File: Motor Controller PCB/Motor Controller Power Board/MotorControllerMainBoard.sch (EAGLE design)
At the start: 59 parts, among them U1 CDBA340L-G

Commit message: Started board work
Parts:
- removed C7, C8: EEUFR1H221B, MotorControllerEagleLibrary:EEUFR1H221B
- removed LED3: (no value), SparkFun (2015_10_14 22_27_04 UTC):LED1206
- removed R12, R9: FKN1WSJR-52-4R7, MotorControllerEagleLibrary:FKN1WSJR-52-4R7
- removed SV1, SV3, SV4: (no value), con-lstb:MA03-1
- removed U$21: (no value), MotorControllerEagleLibrary:AL5809-20S1-7
- added U$24: DA-T263-101E, MotorControllerEagleLibrary:DA-T263-101E
- added U$25: LTN20069, MotorControllerEagleLibrary:LTN20069
- SV2: device con-lstb:MA03-1 -> con-lstb:MA04-1
- U$1, U$2: value NTMFS5C426NT1G -> IPB015N08N5ATMA1; device MotorControllerEagleLibrary:NTMFS5C426NT1G -> MotorControllerEagleLibrary:IPB015N08N5ATMA1
- U$3, U$4: value NTMFS5C426NT1G -> DA-T263-101E; device MotorControllerEagleLibrary:NTMFS5C426NT1G -> MotorControllerEagleLibrary:DA-T263-101E
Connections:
- removed net N$11: R9.22, U$3.GATE
- removed net N$12: R12.22, U$4.GATE
- removed net N$13: R9.11, SV2.2
- removed net N$3: R10.11, SV1.2
- removed net N$4: LED3.C, U$21.A
- removed net N$5: R12.11, SV3.2
- removed net N$8: R11.11, SV4.2
- net 12V_POWER_REGULATED: no longer C7.POSITIVE, C8.POSITIVE
- net 3.3V_ISOLATED: no longer LED3.A
- net FET_DRIVER_SIGNAL: now also R10.11, R11.11; no longer SV1.3, SV2.3, SV3.3, SV4.3
- net GND: now also U$24.GND; no longer C7.NEGATIVE, C8.NEGATIVE, SV1.1, SV2.1, SV3.1, SV6.1, SV6.2, SV6.3, SV6.4, SV7.1, SV7.2, SV7.3, SV7.4, U$3.SOURCE\, U$4.SOURCE\
- net GND_ISOLATED: no longer U$21.C
- net INPUT_POWER(+): now also U$23.GND
- net MOTOR_OUTPUT_(--): now also U$3.GND, U$4.GND; no longer U$3.DRAIN, U$4.DRAIN
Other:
- note added: "HeatSink"

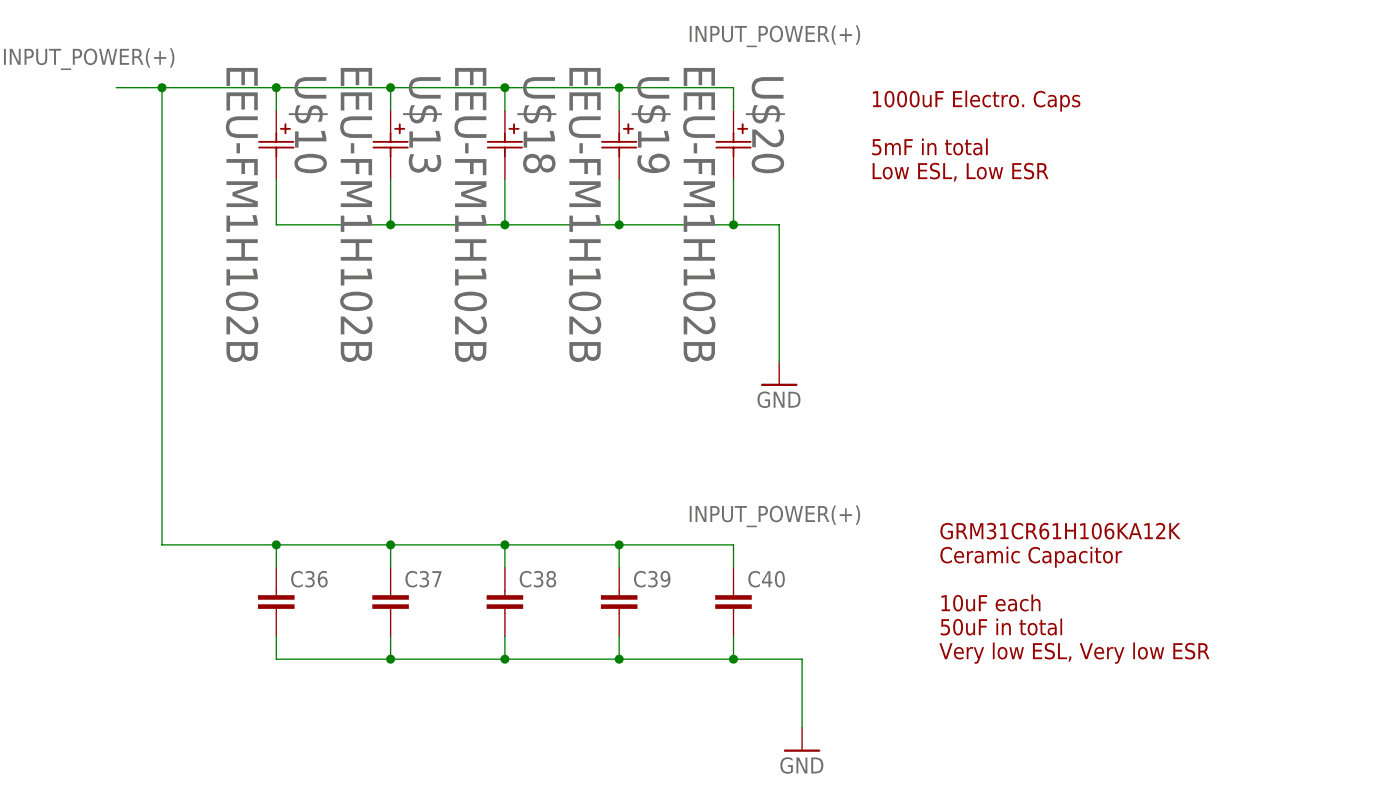
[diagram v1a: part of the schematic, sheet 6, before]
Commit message: shrunk board size to 10x6cm
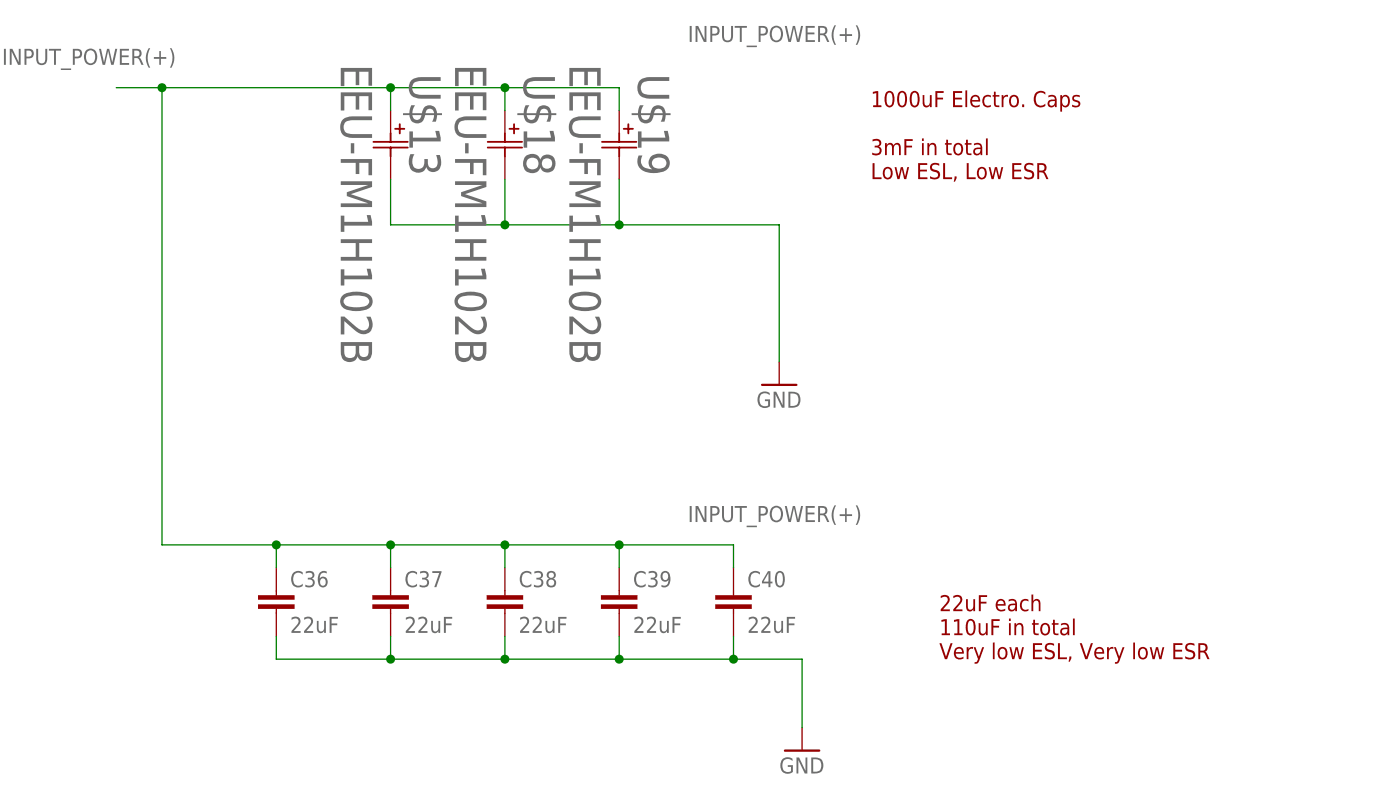
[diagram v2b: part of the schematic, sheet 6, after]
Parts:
- removed U$10, U$20: EEU-FM1H102B, MotorControllerEagleLibrary:EEU-FM1H102B
- C36, C37, C38, C39, C40: value (none) -> 22uF; device resistor:C-EUC1206 -> rcl:C-EUC1210
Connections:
- net GND: no longer U$10.NEGATIVE, U$20.NEGATIVE
- net INPUT_POWER(+): no longer U$10.POSITIVE, U$20.POSITIVE
- net MOTOR_OUTPUT_(+): now also U$9.4; no longer U$9.5
- net POWER_INPUT(+): now also U$9.5; no longer U$9.4
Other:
- note added: "1000uF Electro. Caps 3mF in total Low ESL, Low ESR"
- note added: "22uF each 110uF in total Very low ESL, Very low ESR"
- note removed: "1000uF Electro. Caps 5mF in total Low ESL, Low ESR"
- note removed: "GRM31CR61H106KA12K Ceramic Capacitor 10uF each 50uF in total Very low ESL, Very low ESR"
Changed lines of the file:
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@@
 <part name="GND23" library="E-P-008-R1.2" deviceset="GND" device=""/>
 <part name="GND24" library="SparkFun-Aesthetics" deviceset="GND" device=""/>
-<part name="C36" library="resistor" library_urn="urn:adsk.eagle:library:348" deviceset="C-EU" device="C1206" package3d_urn="urn:adsk.eagle:package:26140/1"/>
-<part name="C37" library="resistor" library_urn="urn:adsk.eagle:library:348" deviceset="C-EU" device="C1206" package3d_urn="urn:adsk.eagle:package:26140/1"/>
-<part name="C38" library="resistor" library_urn="urn:adsk.eagle:library:348" deviceset="C-EU" device="C1206" package3d_urn="urn:adsk.eagle:package:26140/1"/>
-<part name="C39" library="resistor" library_urn="urn:adsk.eagle:library:348" deviceset="C-EU" device="C1206" package3d_urn="urn:adsk.eagle:package:26140/1"/>
-<part name="C40" library="resistor" library_urn="urn:adsk.eagle:library:348" deviceset="C-EU" device="C1206" package3d_urn="urn:adsk.eagle:package:26140/1"/>
+<part name="C36" library="rcl" library_urn="urn:adsk.eagle:library:334" deviceset="C-EU" device="C1210" package3d_urn="urn:adsk.eagle:package:23619/2" value="22uF"/>
+<part name="C37" library="rcl" library_urn="urn:adsk.eagle:library:334" deviceset="C-EU" device="C1210" package3d_urn="urn:adsk.eagle:package:23619/2" value="22uF"/>
+<part name="C38" library="rcl" library_urn="urn:adsk.eagle:library:334" deviceset="C-EU" device="C1210" package3d_urn="urn:adsk.eagle:package:23619/2" value="22uF"/>
+<part name="C39" library="rcl" library_urn="urn:adsk.eagle:library:334" deviceset="C-EU" device="C1210" package3d_urn="urn:adsk.eagle:package:23619/2" value="22uF"/>
+<part name="C40" library="rcl" library_urn="urn:adsk.eagle:library:334" deviceset="C-EU" device="C1210" package3d_urn="urn:adsk.eagle:package:23619/2" value="22uF"/>
 <part name="GND25" library="SparkFun-Aesthetics" deviceset="GND" device=""/>
 <part name="U$12" library="Connector 732-3204" deviceset="732-3204-ND_CONNECTOR" device=""/>
@@
 <part name="PWR_CONFIRM" library="led" library_urn="urn:adsk.eagle:library:259" deviceset="LED" device="CHIPLED_1206" package3d_urn="urn:adsk.eagle:package:15823/2" value="RED"/>
 <part name="GND22" library="E-P-008-R1.2" deviceset="GND" device=""/>
-<part name="U$10" library="MotorControllerEagleLibrary" deviceset="EEU-FM1H102B" device=""/>
 <part name="U$13" library="MotorControllerEagleLibrary" deviceset="EEU-FM1H102B" device=""/>
 <part name="U$18" library="MotorControllerEagleLibrary" deviceset="EEU-FM1H102B" device=""/>
 <part name="U$19" library="MotorControllerEagleLibrary" deviceset="EEU-FM1H102B" device=""/>
-<part name="U$20" library="MotorControllerEagleLibrary" deviceset="EEU-FM1H102B" device=""/>
 <part name="U$8" library="MotorControllerEagleLibrary" deviceset="AL5809-20S1-7" device=""/>
 <part name="LED2" library="SparkFun (2015_10_14 22_27_04 UTC)" deviceset="LED" device="1206"/>
@@
 <net name="POWER_INPUT(+)" class="0">
 <segment>
-<pinref part="U$9" gate="G$1" pin="4"/>
-<wire x1="144.78" y1="83.82" x2="144.78" y2="71.12" width="0.1524" layer="91"/>
-<label x="129.54" y="68.58" size="1.778" layer="95"/>
-</segment>
-</net>
-<net name="MOTOR_OUTPUT_(+)" class="0">
-<segment>
 <pinref part="U$9" gate="G$1" pin="5"/>
 <wire x1="160.02" y1="83.82" x2="160.02" y2="71.12" width="0.1524" layer="91"/>
@@
 <wire x1="175.26" y1="109.22" x2="175.26" y2="106.68" width="0.1524" layer="91"/>
 <label x="175.26" y="104.14" size="1.778" layer="95"/>
+</segment>
+</net>
+<net name="MOTOR_OUTPUT_(+)" class="0">
+<segment>
+<pinref part="U$9" gate="G$1" pin="4"/>
+<wire x1="144.78" y1="83.82" x2="144.78" y2="71.12" width="0.1524" layer="91"/>
+<label x="129.54" y="68.58" size="1.778" layer="95"/>
 </segment>
 </net>
@@
 <plain>
 <text x="195.58" y="27.94" size="3.81" layer="94">Input Filters</text>
-<text x="114.3" y="96.52" size="1.778" layer="94">GRM31CR61H106KA12K
-Ceramic Capacitor
-10uF each
-50uF in total
+<text x="114.3" y="96.52" size="1.778" layer="94">22uF each
+110uF in total
 Very low ESL, Very low ESR</text>
 <text x="106.68" y="149.86" size="1.778" layer="94">1000uF Electro. Caps
-5mF in total
+3mF in total
 Low ESL, Low ESR</text>
 </plain>
@@
 <instance part="C40" gate="G$1" x="91.44" y="104.14"/>
 <instance part="GND25" gate="1" x="99.06" y="86.36"/>
-<instance part="U$10" gate="G$1" x="40.64" y="157.48" rot="R270"/>
 <instance part="U$13" gate="G$1" x="53.34" y="157.48" rot="R270"/>
 <instance part="U$18" gate="G$1" x="66.04" y="157.48" rot="R270"/>
 <instance part="U$19" gate="G$1" x="78.74" y="157.48" rot="R270"/>
-<instance part="U$20" gate="G$1" x="91.44" y="157.48" rot="R270"/>
 </instances>
 <busses>
@@
 <net name="INPUT_POWER(+)" class="0">
 <segment>
-<wire x1="40.64" y1="157.48" x2="40.64" y2="160.02" width="0.1524" layer="91"/>
-<wire x1="40.64" y1="160.02" x2="53.34" y2="160.02" width="0.1524" layer="91"/>
 <wire x1="53.34" y1="160.02" x2="66.04" y2="160.02" width="0.1524" layer="91"/>
 <wire x1="66.04" y1="160.02" x2="78.74" y2="160.02" width="0.1524" layer="91"/>
-<wire x1="78.74" y1="160.02" x2="91.44" y2="160.02" width="0.1524" layer="91"/>
 <wire x1="53.34" y1="160.02" x2="53.34" y2="157.48" width="0.1524" layer="91"/>
 <junction x="53.34" y="160.02"/>
@@
 <junction x="66.04" y="160.02"/>
 <wire x1="78.74" y1="160.02" x2="78.74" y2="157.48" width="0.1524" layer="91"/>
-<junction x="78.74" y="160.02"/>
-<wire x1="91.44" y1="160.02" x2="91.44" y2="157.48" width="0.1524" layer="91"/>
-<wire x1="40.64" y1="160.02" x2="27.94" y2="160.02" width="0.1524" layer="91"/>
-<junction x="40.64" y="160.02"/>
+<wire x1="53.34" y1="160.02" x2="27.94" y2="160.02" width="0.1524" layer="91"/>
 <label x="10.16" y="162.56" size="1.778" layer="95"/>
 <wire x1="27.94" y1="160.02" x2="22.86" y2="160.02" width="0.1524" layer="91"/>
@@
 <label x="86.36" y="111.76" size="1.778" layer="95"/>
 <label x="86.36" y="165.1" size="1.778" layer="95"/>
-<pinref part="U$10" gate="G$1" pin="POSITIVE"/>
 <pinref part="U$13" gate="G$1" pin="POSITIVE"/>
 <pinref part="U$18" gate="G$1" pin="POSITIVE"/>
 <pinref part="U$19" gate="G$1" pin="POSITIVE"/>
-<pinref part="U$20" gate="G$1" pin="POSITIVE"/>
 </segment>
 </net>
 <net name="GND" class="0">
 <segment>
-<wire x1="40.64" y1="149.86" x2="40.64" y2="144.78" width="0.1524" layer="91"/>
-<wire x1="40.64" y1="144.78" x2="53.34" y2="144.78" width="0.1524" layer="91"/>
 <wire x1="53.34" y1="144.78" x2="66.04" y2="144.78" width="0.1524" layer="91"/>
 <wire x1="66.04" y1="144.78" x2="78.74" y2="144.78" width="0.1524" layer="91"/>
-<wire x1="78.74" y1="144.78" x2="91.44" y2="144.78" width="0.1524" layer="91"/>
-<wire x1="91.44" y1="144.78" x2="96.52" y2="144.78" width="0.1524" layer="91"/>
+<wire x1="78.74" y1="144.78" x2="96.52" y2="144.78" width="0.1524" layer="91"/>
 <wire x1="53.34" y1="149.86" x2="53.34" y2="144.78" width="0.1524" layer="91"/>
-<junction x="53.34" y="144.78"/>
 <wire x1="66.04" y1="149.86" x2="66.04" y2="144.78" width="0.1524" layer="91"/>
 <junction x="66.04" y="144.78"/>
 <wire x1="78.74" y1="149.86" x2="78.74" y2="144.78" width="0.1524" layer="91"/>
 <junction x="78.74" y="144.78"/>
-<wire x1="91.44" y1="149.86" x2="91.44" y2="144.78" width="0.1524" layer="91"/>
-<junction x="91.44" y="144.78"/>
 <pinref part="GND24" gate="1" pin="GND"/>
 <wire x1="96.52" y1="144.78" x2="96.52" y2="129.54" width="0.1524" layer="91"/>
-<pinref part="U$10" gate="G$1" pin="NEGATIVE"/>
 <pinref part="U$13" gate="G$1" pin="NEGATIVE"/>
 <pinref part="U$18" gate="G$1" pin="NEGATIVE"/>
 <pinref part="U$19" gate="G$1" pin="NEGATIVE"/>
-<pinref part="U$20" gate="G$1" pin="NEGATIVE"/>
-</segment>
-<segment>
+</segment>
+<segment>
